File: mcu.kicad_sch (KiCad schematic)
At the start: 1 part, among them U1 ESP32-C6-MINI-1

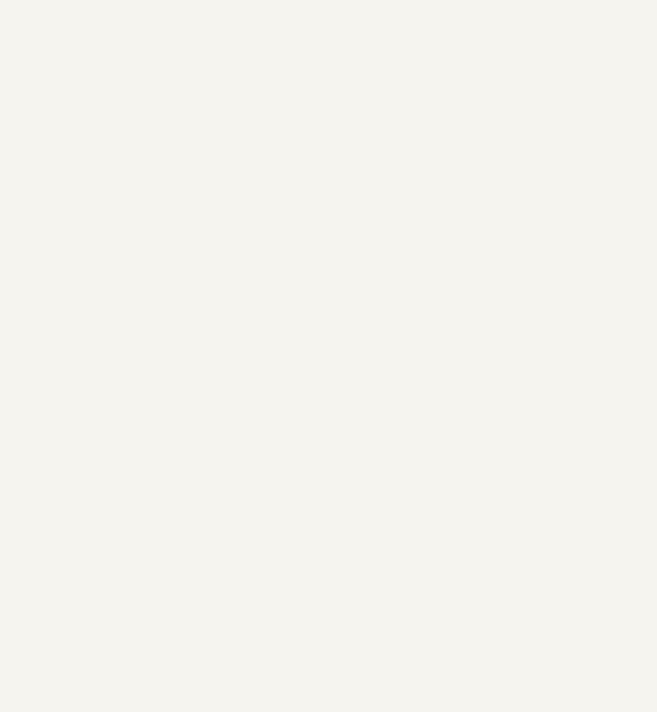
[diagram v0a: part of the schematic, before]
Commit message: added usb to uart converter
started wiring self powering configuration
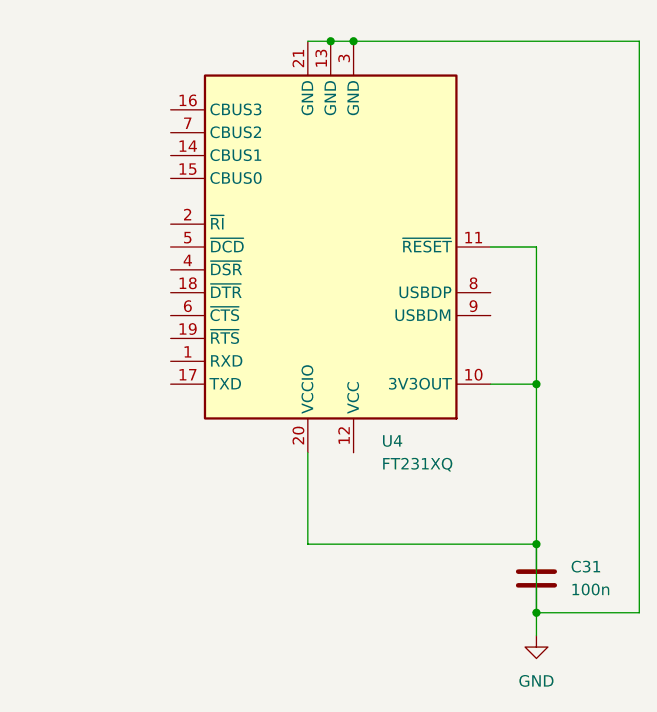
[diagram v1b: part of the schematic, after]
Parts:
- added C31: 100n, symbol Device:C
- added U4: FT231XQ, Package_DFN_QFN:QFN-20-1EP_4x4mm_P0.5mm_EP2.5x2.5mm, symbol Interface_USB:FT231XQ
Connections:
- new net GND: C31.1, C31.2, U4.10 (3V3OUT), U4.11 (~{RESET}), U4.13 (GND), U4.20 (VCCIO), U4.21 (GND), U4.3 (GND)

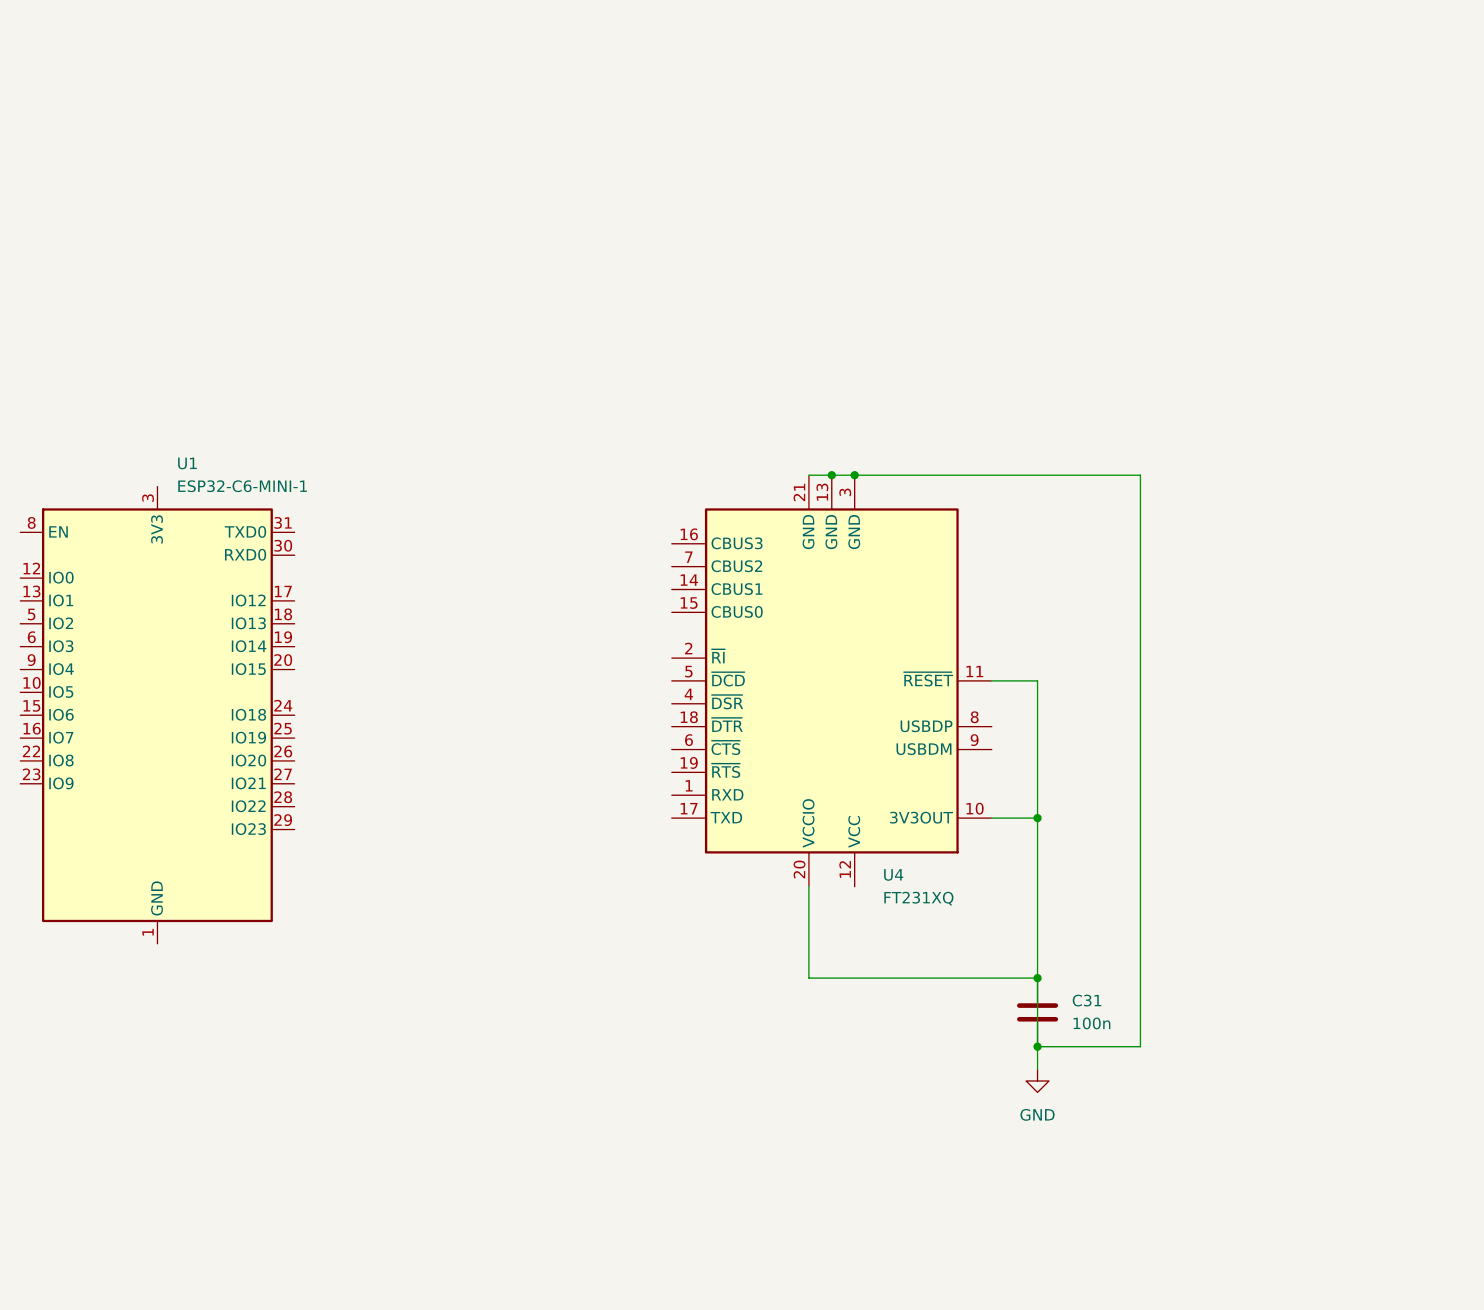
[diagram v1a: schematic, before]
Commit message: self powering configuration
finished self power configuration of usb uart converter
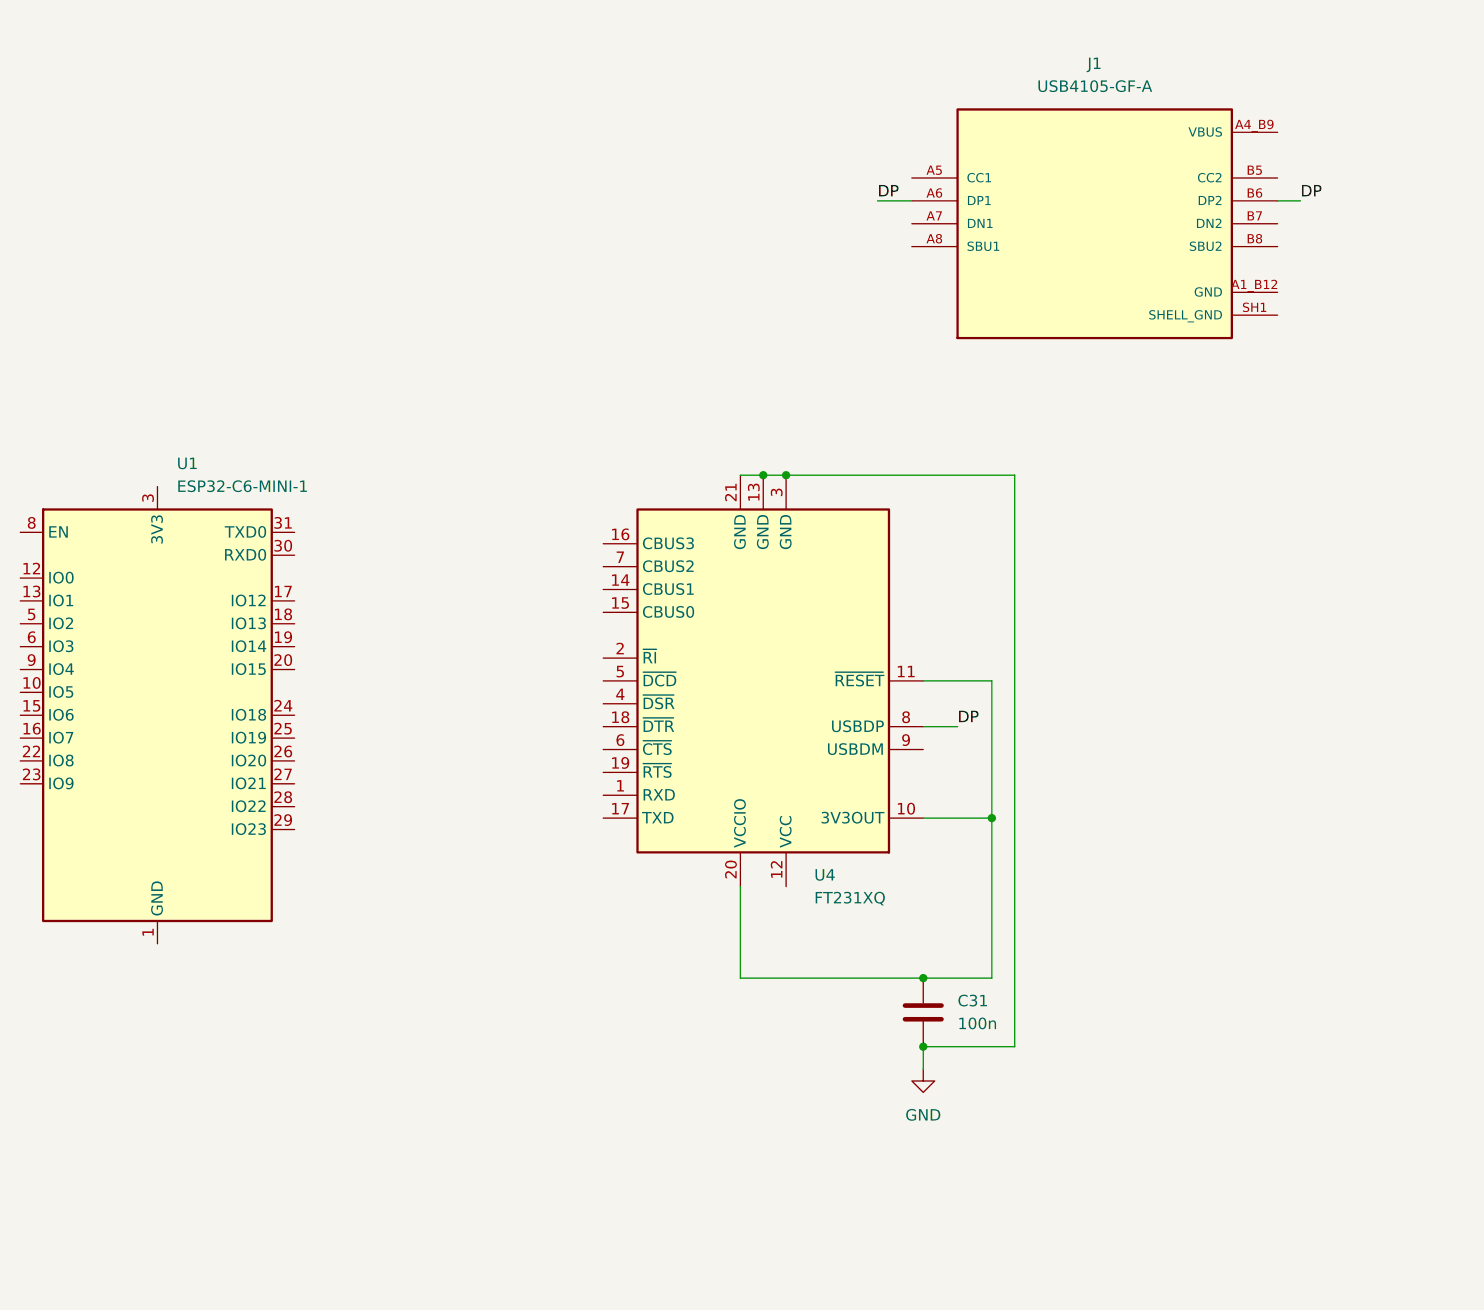
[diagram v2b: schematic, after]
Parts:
- added J1: USB4105-GF-A, USB4105-GF-A:GCT_USB4105-GF-A, symbol USB4105-GF-A:USB4105-GF-A
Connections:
- net GND: now also J1.A1_B12 (GND), J1.B1_A12 (GND); no longer C31.2, U4.10 (3V3OUT), U4.11 (~{RESET}), U4.20 (VCCIO)
- net DP: now reaches U4.8 (USBDP)
- net DP: now also J1.A6 (DP1), J1.B6 (DP2)
- new net: C31.2, U4.10 (3V3OUT), U4.11 (~{RESET}), U4.20 (VCCIO)
- new net SHELL_GND: J1.SH1 (SHELL_GND), J1.SH2 (SHELL_GND), J1.SH3 (SHELL_GND), J1.SH4 (SHELL_GND)
- new net VBUS: J1.A4_B9 (VBUS), J1.B4_A9 (VBUS)
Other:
- moved on the sheet: C31, U4

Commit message: finished self powered configuration
finished self powered configuration of usb uart converter (correctly saved)
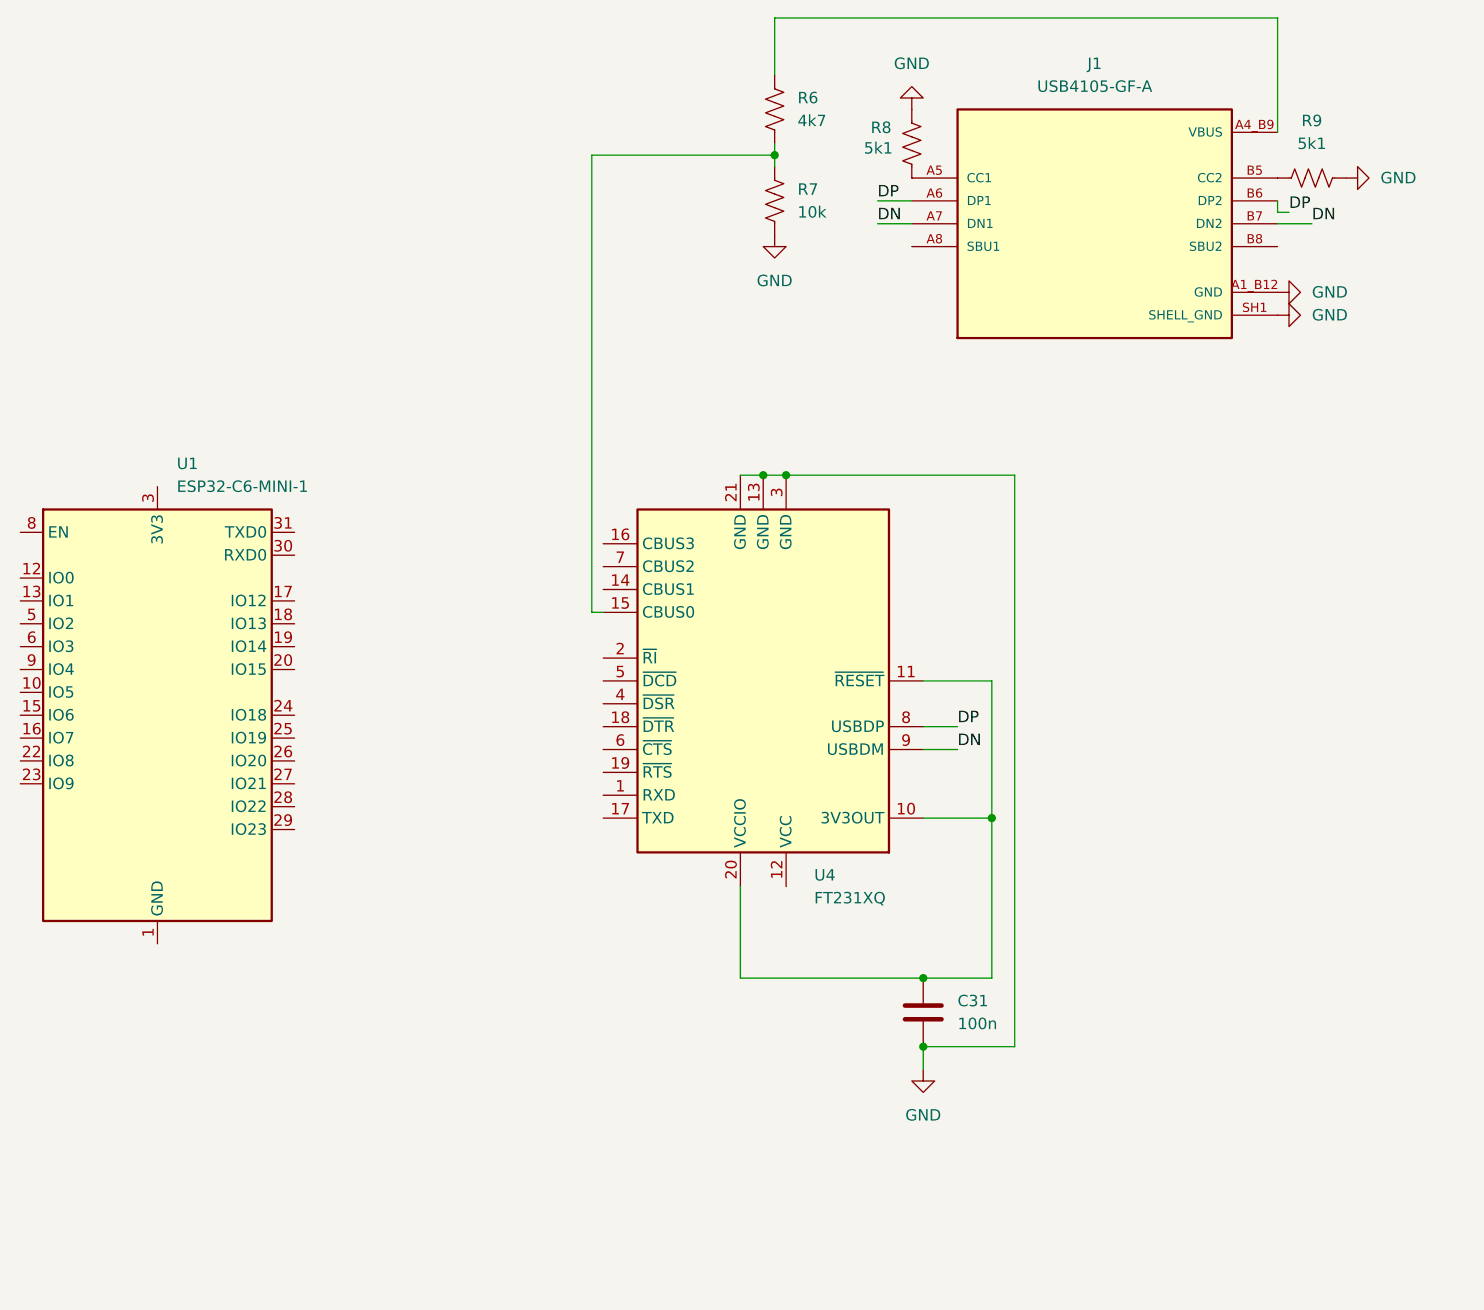
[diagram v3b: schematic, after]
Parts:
- added R6: 4k7, symbol Device:R_US
- added R7: 10k, symbol Device:R_US
- added R8, R9: 5k1, symbol Device:R_US
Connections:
- net SHELL_GND is gone; now on net GND: J1.SH1 (SHELL_GND), J1.SH2 (SHELL_GND), J1.SH3 (SHELL_GND), J1.SH4 (SHELL_GND)
- net GND: now also R7.2, R8.1, R9.2
- net VBUS: now also R6.1
- net at J1.A5 (CC1): now also R8.2
- net DN: now reaches J1.A7 (DN1)
- net DN: now also J1.B7 (DN2), U4.9 (USBDM)
- net at J1.B5 (CC2): now also R9.1
- net at U4.15 (CBUS0): now also R6.2, R7.1

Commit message: proper formating
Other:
- moved on the sheet: R6, R7, R8, R9

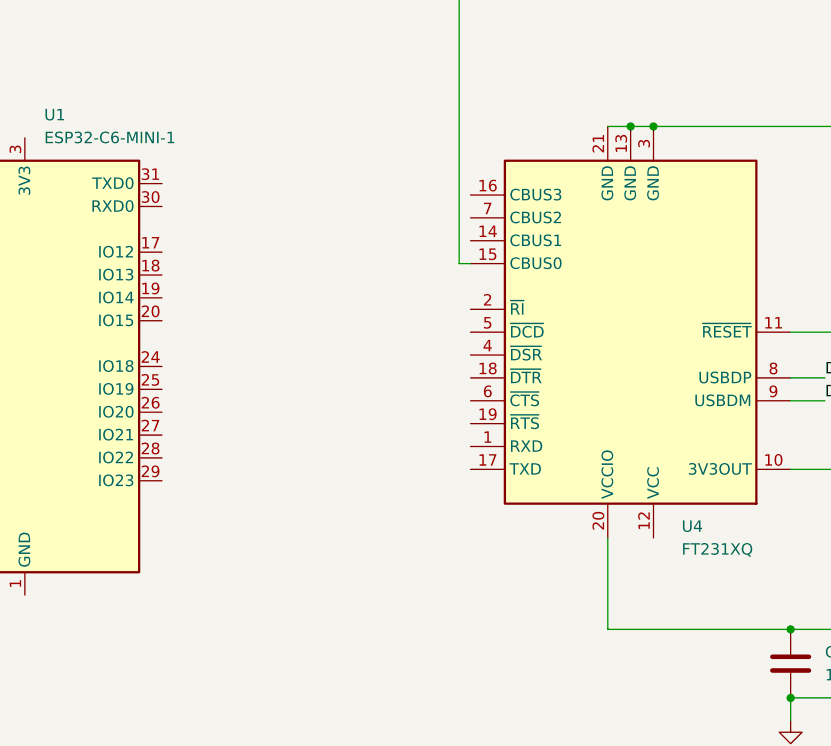
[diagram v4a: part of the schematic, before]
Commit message: Added TX-RX wiring
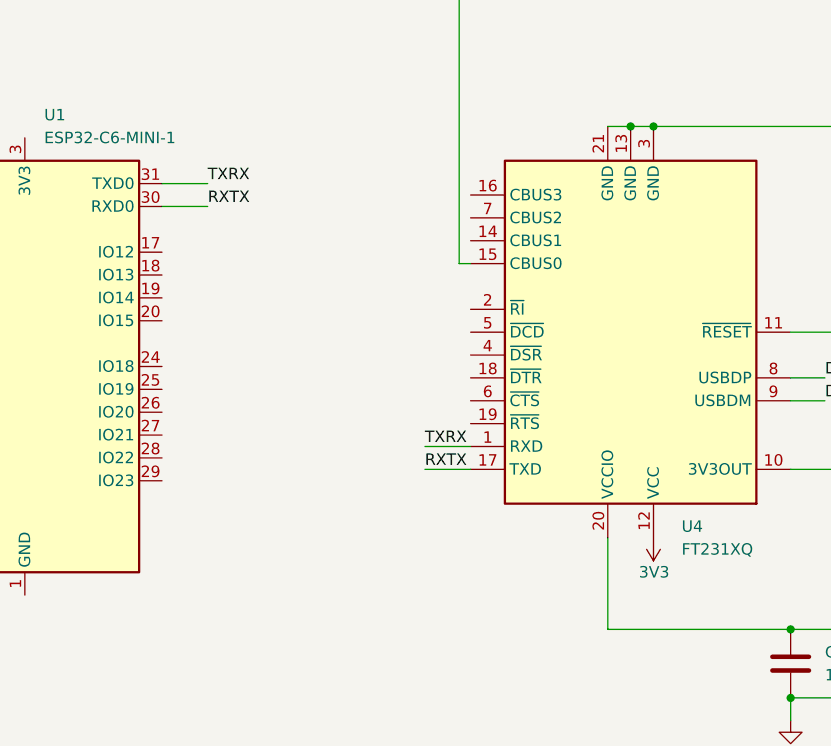
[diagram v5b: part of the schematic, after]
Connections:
- net RXTX: now reaches U1.30 (RXD0)
- net RXTX: now also U4.17 (TXD)
- net TXRX: now reaches U1.31 (TXD0)
- net TXRX: now also U4.1 (RXD)
- net 3V3: now reaches U4.12 (VCC)
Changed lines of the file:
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@@
+	(wire
+		(pts
+			(xy 157.48 72.39) (xy 152.4 72.39)
+		)
+		(stroke
+			(width 0)
+			(type default)
+		)
+	)
 	(wire
 		(pts
@@
 	(wire
 		(pts
+			(xy 152.4 74.93) (xy 157.48 74.93)
+		)
+		(stroke
+			(width 0)
+			(type default)
+		)
+	)
+	(wire
+		(pts
 			(xy 217.17 38.1) (xy 220.98 38.1)
 		)
@@
 	(wire
 		(pts
+			(xy 181.61 104.14) (xy 186.69 104.14)
+		)
+		(stroke
+			(width 0)
+			(type default)
+		)
+	)
+	(wire
+		(pts
 			(xy 222.25 93.98) (xy 226.06 93.98)
 		)
@@
 	(wire
 		(pts
+			(xy 181.61 101.6) (xy 186.69 101.6)
+		)
+		(stroke
+			(width 0)
+			(type default)
+		)
+	)
+	(wire
+		(pts
 			(xy 222.25 129.54) (xy 232.41 129.54)
 		)
@@
 			(width 0)
 			(type default)
+		)
+	)
+	(label "RXTX"
+		(at 181.61 104.14 0)
+		(effects
+			(font
+				(size 1.27 1.27)
+			)
+			(justify left bottom)
 		)
 	)
@@
 		)
 	)
+	(label "RXTX"
+		(at 157.48 74.93 0)
+		(effects
+			(font
+				(size 1.27 1.27)
+			)
+			(justify left bottom)
+		)
+	)
+	(label "TXRX"
+		(at 157.48 72.39 0)
+		(effects
+			(font
+				(size 1.27 1.27)
+			)
+			(justify left bottom)
+		)
+	)
 	(label "DP"
 		(at 265.43 35.56 0)
+		(effects
+			(font
+				(size 1.27 1.27)
+			)
+			(justify left bottom)
+		)
+	)
+	(label "TXRX"
+		(at 181.61 101.6 0)
 		(effects
 			(font
@@
 					(unit 1)
 				)
+			)
+		)
+	)
+	(symbol
+		(lib_id "power:+1V0")
+		(at 207.01 111.76 180)
+		(unit 1)
+		(exclude_from_sim no)
+		(in_bom yes)
+		(on_board yes)
+		(dnp no)
+		(property "Reference" "#PWR037"
+			(at 207.01 107.95 0)
+			(effects
+				(font
+					(size 1.27 1.27)
+				)
+				(hide yes)
+			)
+		)
+		(property "Value" "3V3"
+			(at 208.788 115.57 0)
+			(effects
+				(font
+					(size 1.27 1.27)
+				)
+				(justify left)
+			)
+		)
+		(property "Footprint" ""
+			(at 207.01 111.76 0)
+			(effects
+				(font
+					(size 1.27 1.27)
+				)
+				(hide yes)
+			)
+		)
+		(property "Datasheet" ""
+			(at 207.01 111.76 0)
+			(effects
+				(font
+					(size 1.27 1.27)
+				)
+				(hide yes)
+			)
+		)
+		(property "Description" "Power symbol creates a global label with name \"+1V0\""
+			(at 207.01 111.76 0)
+			(effects
+				(font
+					(size 1.27 1.27)
+				)
+				(hide yes)
+			)
+		)
+		(pin "1"
+		)
+		(instances
+			(project "PALReceiver"
+				(path "/2785bbdd-da8c-4c23-b498-605d17251f95/329eb62d-f8d8-4a30-9cb6-995f07524828"
+					(reference "#PWR037")
+					(unit 1)
+				)
